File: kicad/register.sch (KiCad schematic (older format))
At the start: 11 parts, among them U7 74LS173, U8 74LS173, U9 74LS245

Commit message: bugfixed design
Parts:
- renumbered U7 to U14, U8 to U15, U9 to U16
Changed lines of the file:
@@
 LIBS:valves
 LIBS:switches
-LIBS:74xxx
-LIBS:28c16
 LIBS:sap-be-cache
-EELAYER 24 0
+EELAYER 25 0
 EELAYER END
 $Descr A4 11693 8268
@@
 $EndDescr
 $Comp
-L 74LS173 U7
+L 74LS173 U14
 U 1 1 590A45FD
 P 4950 2450
-AR Path="/590AA801/590A45FD" Ref="U7"  Part="1"
-AR Path="/590A2A35/590A45FD" Ref="U10"  Part="1"
-F 0 "U10" H 5050 2550 50  0000 C CNN
+AR Path="/590AA801/590A45FD" Ref="U14"  Part="1"
+AR Path="/590A2A35/590A45FD" Ref="U17"  Part="1"
+F 0 "U17" H 5050 2550 50  0000 C CNN
 F 1 "74LS173" H 5050 2400 50  0000 C CNN
 F 2 "Housings_DIP:DIP-16_W7.62mm_LongPads" H 4950 2450 50  0001 C CNN
@@
 $EndComp
 $Comp
-L 74LS173 U8
+L 74LS173 U15
 U 1 1 590A4604
 P 4950 3800
-AR Path="/590AA801/590A4604" Ref="U8"  Part="1"
-AR Path="/590A2A35/590A4604" Ref="U11"  Part="1"
-F 0 "U11" H 5050 3900 50  0000 C CNN
+AR Path="/590AA801/590A4604" Ref="U15"  Part="1"
+AR Path="/590A2A35/590A4604" Ref="U18"  Part="1"
+F 0 "U18" H 5050 3900 50  0000 C CNN
 F 1 "74LS173" H 5050 3750 50  0000 C CNN
 F 2 "Housings_DIP:DIP-16_W7.62mm_LongPads" H 4950 3800 50  0001 C CNN
@@
 $EndComp
 $Comp
-L 74LS245 U9
+L 74LS245 U16
 U 1 1 591439A0
 P 7350 3000
-AR Path="/590AA801/591439A0" Ref="U9"  Part="1"
-AR Path="/590A2A35/591439A0" Ref="U12"  Part="1"
-F 0 "U12" H 7450 3575 50  0000 L BNN
+AR Path="/590AA801/591439A0" Ref="U16"  Part="1"
+AR Path="/590A2A35/591439A0" Ref="U19"  Part="1"
+F 0 "U19" H 7450 3575 50  0000 L BNN
 F 1 "74LS245" H 7400 2425 50  0000 L TNN
 F 2 "Housings_DIP:DIP-20_W7.62mm_LongPads" H 7350 3000 50  0001 C CNN
@@
 ~LOAD
 $Comp
-L GND #PWR025
+L GND #PWR24
 U 1 1 591439AA
 P 8650 4700
-AR Path="/590AA801/591439AA" Ref="#PWR025"  Part="1"
-AR Path="/590A2A35/591439AA" Ref="#PWR027"  Part="1"
-F 0 "#PWR027" H 8650 4450 50  0001 C CNN
+AR Path="/590AA801/591439AA" Ref="#PWR24"  Part="1"
+AR Path="/590A2A35/591439AA" Ref="#PWR26"  Part="1"
+F 0 "#PWR26" H 8650 4450 50  0001 C CNN
 F 1 "GND" H 8650 4550 50  0000 C CNN
 F 2 "" H 8650 4700 50  0000 C CNN
@@
 	3600 1600 3100 1600
 $Comp
-L VCC #PWR028
+L VCC #PWR23
 U 1 1 59141563
 P 6550 3400
-AR Path="/590A2A35/59141563" Ref="#PWR028"  Part="1"
-AR Path="/590AA801/59141563" Ref="#PWR026"  Part="1"
-F 0 "#PWR028" H 6550 3250 50  0001 C CNN
+AR Path="/590AA801/59141563" Ref="#PWR23"  Part="1"
+AR Path="/590A2A35/59141563" Ref="#PWR25"  Part="1"
+F 0 "#PWR25" H 6550 3250 50  0001 C CNN
 F 1 "VCC" H 6550 3550 50  0000 C CNN
 F 2 "" H 6550 3400 50  0000 C CNN

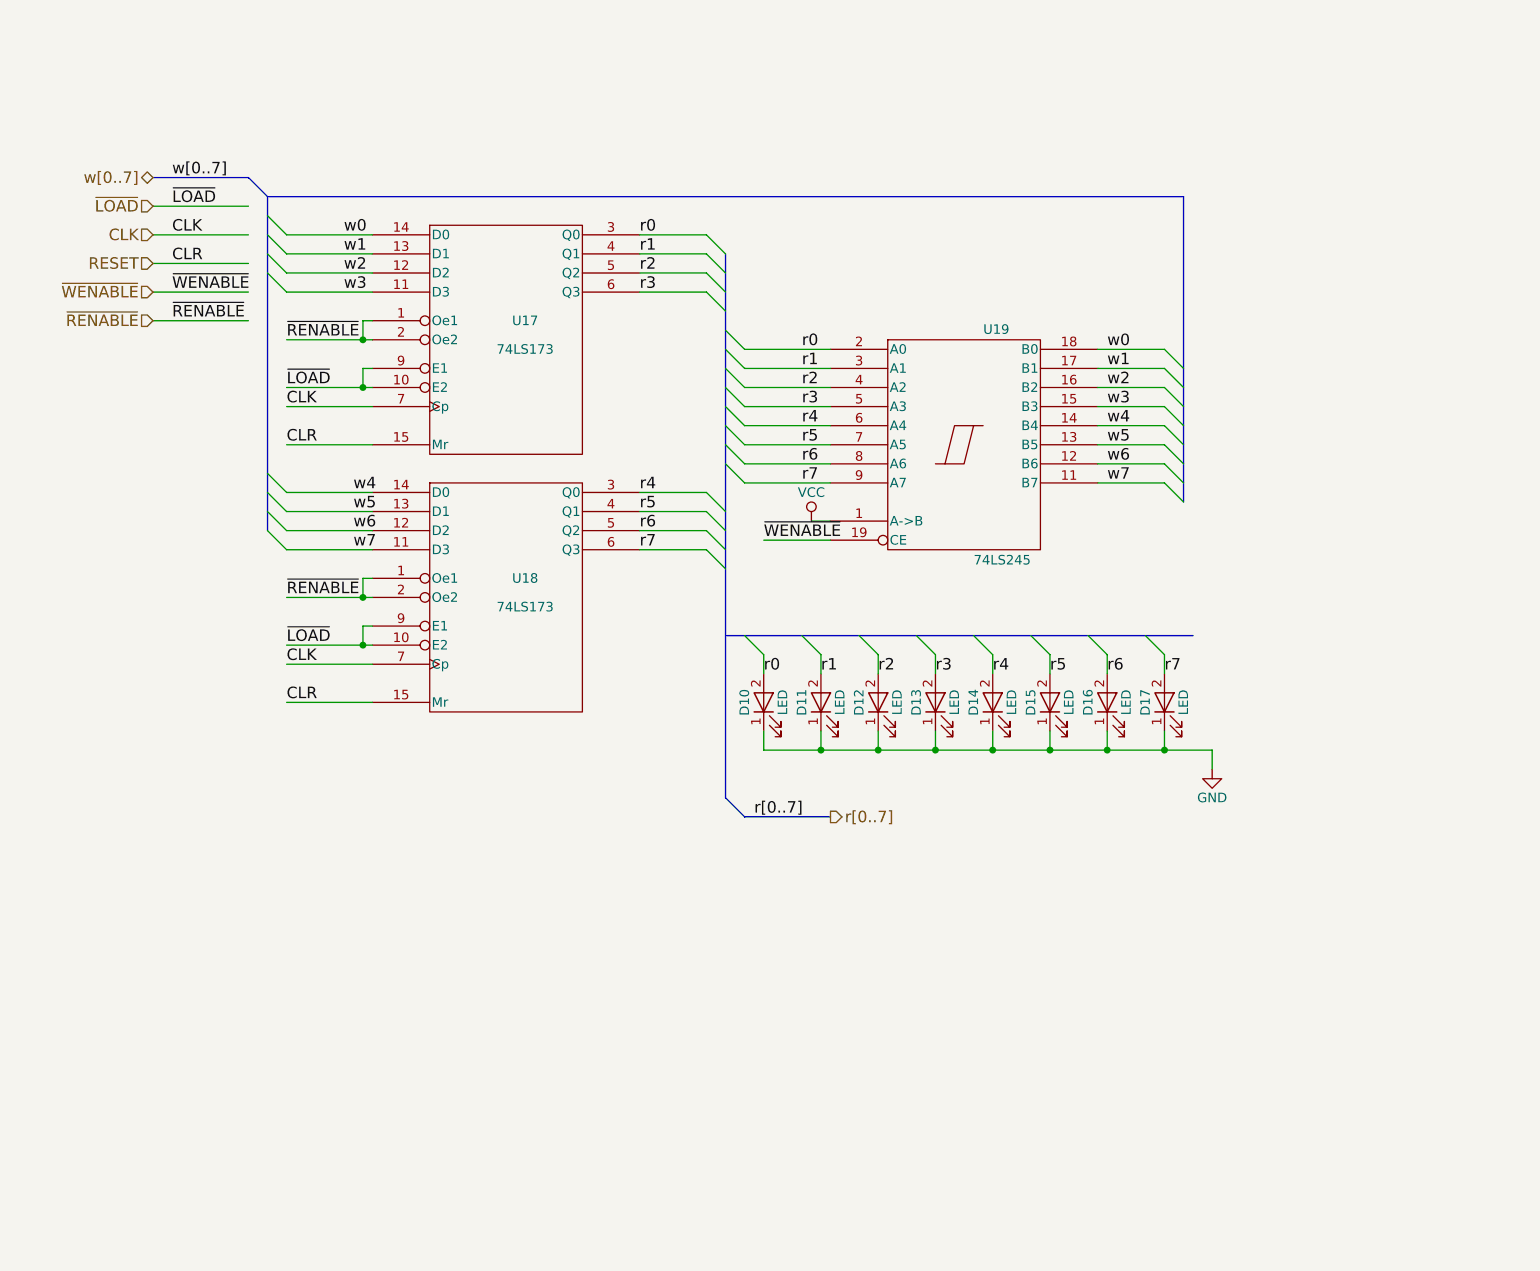
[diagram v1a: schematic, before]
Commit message: Update bugfix version to use updated kicad libraries
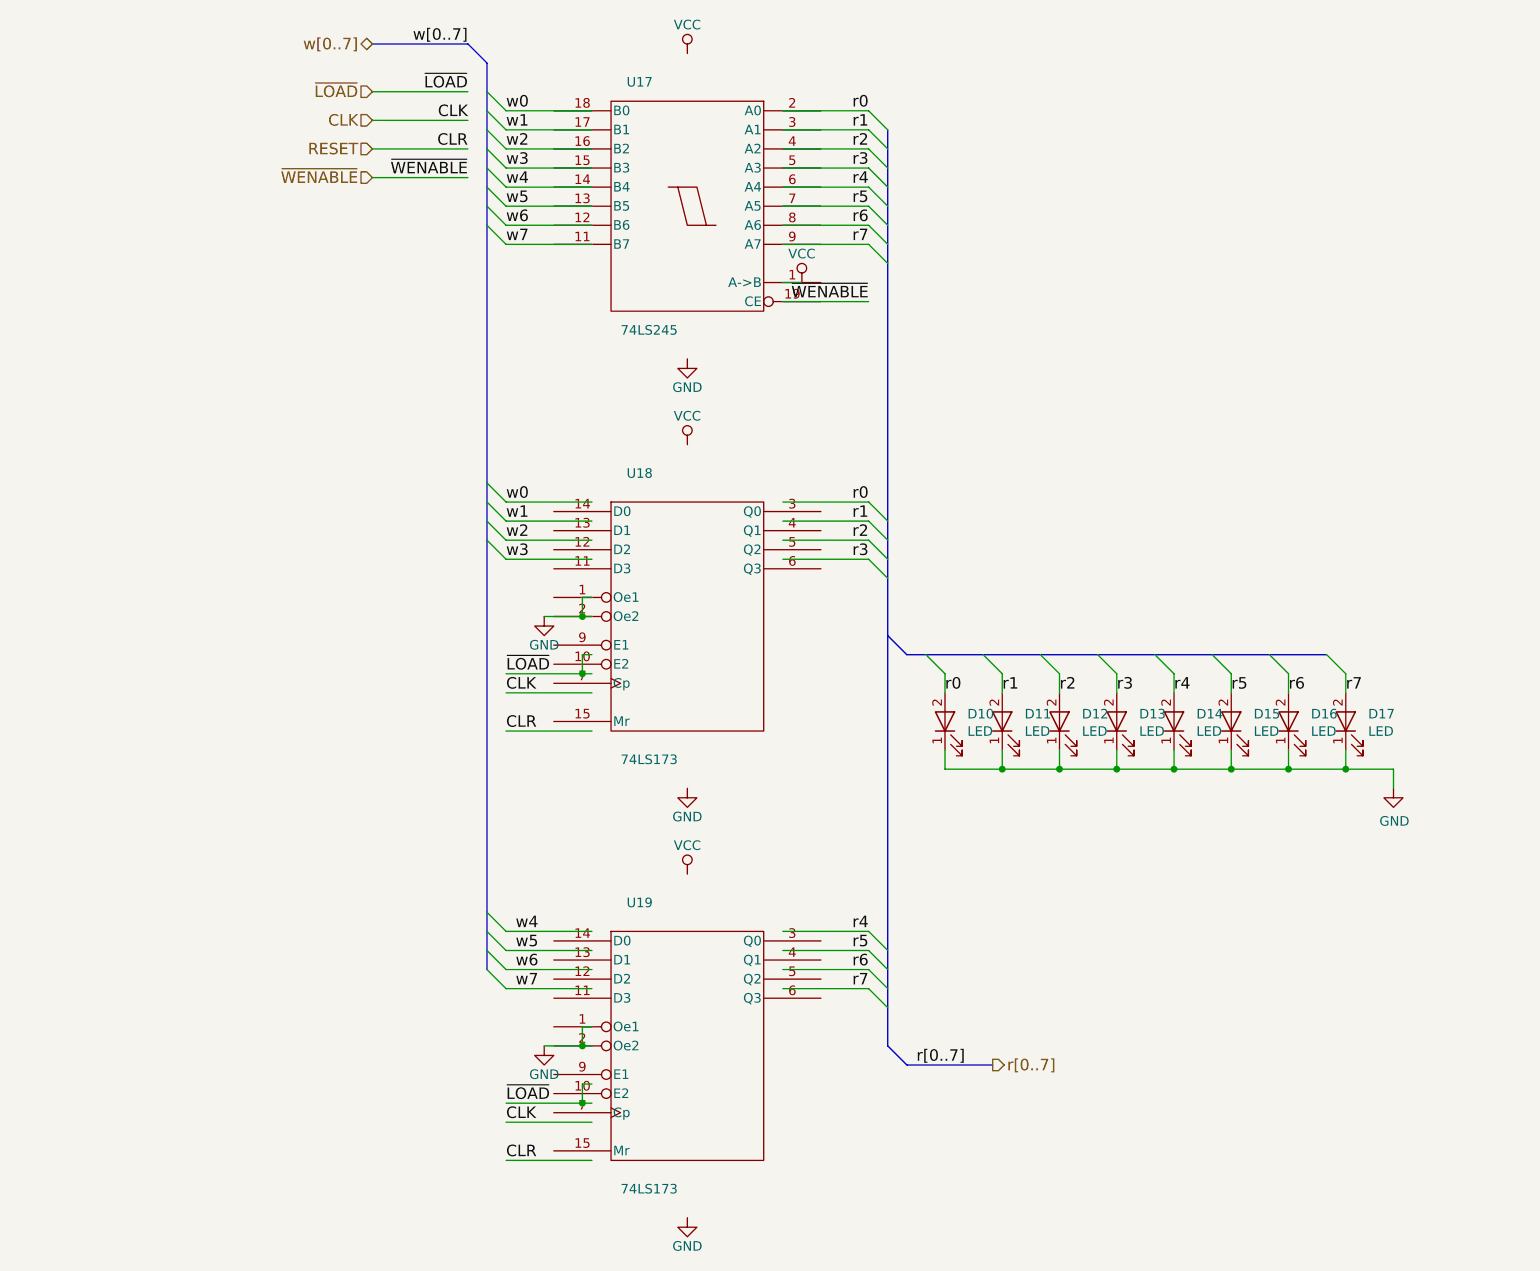
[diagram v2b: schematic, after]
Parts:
- removed D2, D3, D4, D5, D6, D7, D8, D9: LED, LEDs:LED-5MM, symbol LED
- removed U14, U15: 74LS173, Housings_DIP:DIP-16_W7.62mm_LongPads, symbol 74LS173
- removed U16: 74LS245, Housings_DIP:DIP-20_W7.62mm_LongPads, symbol 74LS245
- added D10, D11, D12, D13, D14, D15, D16, D17: LED, symbol Device:LED
- added U17: 74LS245, symbol 74xx:74LS245
- added U18, U19: 74LS173, symbol 74xx:74LS173
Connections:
- net labels removed: ~RENABLE
- wire segments 73 -> 83

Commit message: update bus names and improve sheet text
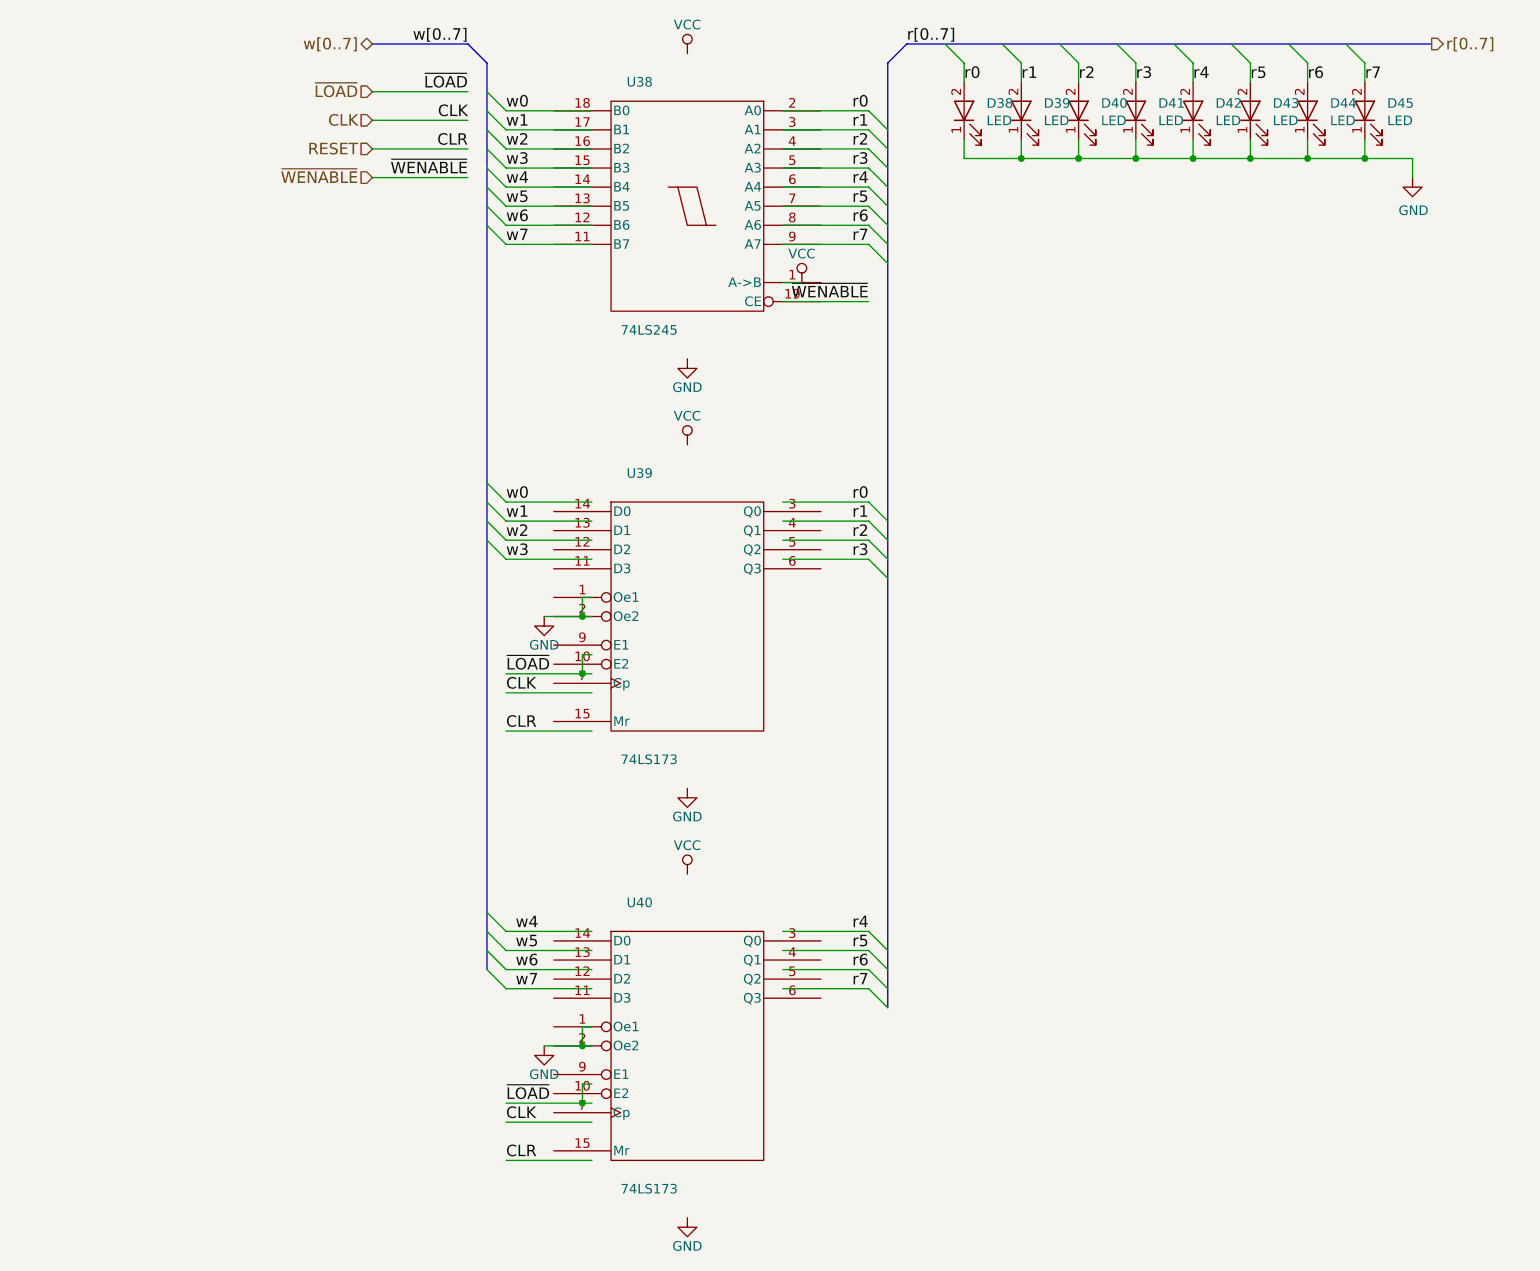
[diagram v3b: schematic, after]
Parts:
- renumbered D10 to D20, D11 to D21, D12 to D22, D13 to D23, D14 to D24, D15 to D25, D16 to D26, D17 to D27, U17 to U24, U18 to U25, U19 to U26
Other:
- moved on the sheet: D38, D39, D40, D41, D42, D43, D44, D45
